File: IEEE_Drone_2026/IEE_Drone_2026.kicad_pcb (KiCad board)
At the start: 4 copper layers, 44.9 x 45.5 mm, 44 parts, among them IC1 TPSM84209RKHT, J1 ESC, J13 USB_C_Receptacle_USB2.0_16P, J2 M4 Mounting, J3 M4 Mounting, J4 M4 Mounting, J5 M4 Mounting, U2 STM32F405RGTx, U3 BMP390, U5 LIS2MDL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

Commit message: slight routing updates
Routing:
- net GND: track 78.0 -> 76.6 mm, vias 24 -> 23
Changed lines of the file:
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@@
-	)
-	(segment
-		(start 85.2086 110.8384)
-		(end 83.853 110.8384)
-		(width 0.7)
-		(layer "F.Cu")
-		(net 1)
 	)
 	(segment
@@
 		(end 95.949062 114.178337)
 		(width 0.3)
-		(layer "F.Cu")
-		(net 1)
-	)
-	(segment
-		(start 83.853 110.8384)
-		(end 83.8494 110.8348)
-		(width 0.7)
 		(layer "F.Cu")
 		(net 1)
@@
 		(size 0.6)
 		(drill 0.3)
-		(layers "F.Cu" "B.Cu")
-		(net 1)
-	)
-	(via
-		(at 83.8494 110.8348)
-		(size 0.6)
-		(drill 0.3)

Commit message: slight routing updates
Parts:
- moved C8 1.09 mm to (90.3, 111.4), turned to 0 degrees
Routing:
- net Net-(U2-PC14): track 4.42 -> 2.35 mm
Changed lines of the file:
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@@
 	(footprint "Capacitor_SMD:C_0603_1608Metric_Pad1.08x0.95mm_HandSolder"
 		(layer "F.Cu")
-		(at 89.3042 111.8192 -90)
+		(at 90.297 111.379)
 		(descr "Capacitor SMD 0603 (1608 Metric), square (rectangular) end terminal, IPC-7351 nominal with elongated pad for handsoldering. (Body size source: IPC-SM-782 page 76, https://www.pcb-3d.com/wordpress/wp-content/uploads/ipc-sm-782a_amendment_1_and_2.pdf), generated with kicad-footprint-generator")
 		(tags "capacitor handsolder")
 		(property "Reference" "C8"
-			(at 2.3538 0.0232 180)
+			(at -0.127 1.524 180)
 			(layer "F.SilkS")
 			(effects
@@
 		)
 		(property "Value" "12pF"
-			(at 0 1.43 90)
+			(at 0 1.43 0)
 			(layer "F.Fab")
 			(hide yes)
@@
 		)
 		(property "Datasheet" "~"
-			(at 0 0 90)
+			(at 0 0 0)
 			(layer "F.Fab")
 			(hide yes)
@@
 		)
 		(property "Description" "Unpolarized capacitor"
-			(at 0 0 90)
+			(at 0 0 0)
 			(layer "F.Fab")
 			(hide yes)
@@
 		(attr smd)
 		(fp_line
-			(start -0.146267 0.51)
-			(end 0.146267 0.51)
+			(start -0.146267 -0.51)
+			(end 0.146267 -0.51)
 			(stroke
 				(width 0.12)
@@
 		)
 		(fp_line
-			(start -0.146267 -0.51)
-			(end 0.146267 -0.51)
+			(start -0.146267 0.51)
+			(end 0.146267 0.51)
 			(stroke
 				(width 0.12)
@@
 		)
 		(fp_line
-			(start -1.65 0.73)
-			(end -1.65 -0.73)
+			(start -1.65 -0.73)
+			(end 1.65 -0.73)
 			(stroke
 				(width 0.05)
@@
 		)
 		(fp_line
-			(start 1.65 0.73)
-			(end -1.65 0.73)
+			(start -1.65 0.73)
+			(end -1.65 -0.73)
 			(stroke
 				(width 0.05)
@@
 		)
 		(fp_line
-			(start -1.65 -0.73)
-			(end 1.65 -0.73)
+			(start 1.65 -0.73)
+			(end 1.65 0.73)
 			(stroke
 				(width 0.05)
@@
 		)
 		(fp_line
-			(start 1.65 -0.73)
-			(end 1.65 0.73)
+			(start 1.65 0.73)
+			(end -1.65 0.73)
 			(stroke
 				(width 0.05)
@@
 		)
 		(fp_line
-			(start -0.8 0.4)
-			(end -0.8 -0.4)
+			(start -0.8 -0.4)
+			(end 0.8 -0.4)
 			(stroke
 				(width 0.1)
@@
 		)
 		(fp_line
-			(start 0.8 0.4)
-			(end -0.8 0.4)
+			(start -0.8 0.4)
+			(end -0.8 -0.4)
 			(stroke
 				(width 0.1)
@@
 		)
 		(fp_line
-			(start -0.8 -0.4)
-			(end 0.8 -0.4)
+			(start 0.8 -0.4)
+			(end 0.8 0.4)
 			(stroke
 				(width 0.1)
@@
 		)
 		(fp_line
-			(start 0.8 -0.4)
-			(end 0.8 0.4)
+			(start 0.8 0.4)
+			(end -0.8 0.4)
 			(stroke
 				(width 0.1)
@@
 		)
 		(fp_text user "${REFERENCE}"
-			(at 0 0 90)
+			(at 0 0 0)
 			(layer "F.Fab")
 			(effects
@@
 		)
 		(pad "1" smd roundrect
-			(at -0.8625 0 270)
+			(at -0.8625 0)
 			(size 1.075 0.95)
 			(layers "F.Cu" "F.Mask" "F.Paste")
@@
 		)
 		(pad "2" smd roundrect
-			(at 0.8625 0 270)
+			(at 0.8625 0)
 			(size 1.075 0.95)
 			(layers "F.Cu" "F.Mask" "F.Paste")
@@
 	)
 	(segment
-		(start 87.6086 110.8384)
-		(end 89.1859 110.8384)
-		(width 0.3)
+		(start 88.1492 111.379)
+		(end 87.6086 110.8384)
+		(width 0.2)
 		(layer "F.Cu")
 		(net 8)
 	)
 	(segment
+		(start 89.4345 111.379)
+		(end 88.1492 111.379)
+		(width 0.2)
+		(layer "F.Cu")
+		(net 8)
+	)
+	(segment
+		(start 91.1595 110.8264)
+		(end 91.1595 111.379)
+		(width 0.3)
+		(layer "F.Cu")
+		(net 9)
+	)
+	(segment
 		(start 91.615 110.3709)
-		(end 89.3042 112.6817)
+		(end 91.1595 110.8264)
 		(width 0.3)
 		(layer "F.Cu")

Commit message: complete redesign
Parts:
- removed BOOT0, NRST: TestPoint, TestPoint:TestPoint_Loop_D2.50mm_Drill1.0mm
- GPS1: footprint Connector_PinHeader_2.54mm:PinHeader_1x04_P2.54mm_Vertical -> Connector_JST:JST_SH_BM04B-SRSS-TB_1x04-1MP_P1.00mm_Vertical
- Pixy1: footprint Connector_PinSocket_2.54mm:PinSocket_1x05_P2.54mm_Vertical -> Connector_JST:JST_SH_BM05B-SRSS-TB_1x05-1MP_P1.00mm_Vertical
- RF1: footprint Connector_PinHeader_2.54mm:PinHeader_1x08_P2.54mm_Vertical -> Connector_JST:JST_SH_BM09B-SRSS-TB_1x09-1MP_P1.00mm_Vertical
- moved GPS1 96.3 mm to (156.7, 138.6), turned to -90 degrees
- moved C19 90.0 mm to (150.4, 153.5), turned to 180 degrees
- moved C22 89.7 mm to (150.4, 155.0), turned to 180 degrees
- moved C16 82.5 mm to (153.9, 144.6)
- moved Y2 81.1 mm to (157.4, 152.4), turned to 90 degrees
- moved C8 80.1 mm to (156.6, 156.4), turned to 180 degrees
- moved C18 78.5 mm to (150.0, 138.2), turned to 0 degrees
- moved C7 77.5 mm to (157.6, 148.3), turned to 180 degrees
- moved R8 76.5 mm to (131.5, 154.0), turned to 180 degrees
- moved C15 75.3 mm to (140.2, 152.0)
- moved R6 73.6 mm to (130.5, 149.5), turned to -90 degrees
- moved Pixy1 73.2 mm to (135.5, 130.3), turned to 0 degrees
- moved C20 71.3 mm to (137.8, 149.2)
- moved J13 71.3 mm to (124.2, 152.7), turned to -90 degrees
- moved J3 69.5 mm to (122.2, 129.9)
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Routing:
- net +3.3V: track 103.1 -> 64.6 mm, vias 16 -> 15
- net /MISO: track 67.9 -> 29.9 mm, vias 2 -> 4
- net /MOSI: track 71.7 -> 40.5 mm
- net /PB12: track 50.3 -> 20.3 mm, vias 3 -> 4
- net +VDC: track 77.7 -> 50.2 mm
- net /SCK: track 41.9 -> 16.1 mm, vias 4 -> 0
- net /TX: track 30.5 -> 5.37 mm, vias 1 -> 0
- net /RX: track 30.2 -> 6.00 mm, vias 1 -> 0
- net GND: track 76.6 -> 98.1 mm, vias 23 -> 26
- net /PB13: track 40.8 -> 19.4 mm, vias 4 -> 2
- net /PB3: track 40.1 -> 18.7 mm, vias 0 -> 3
- net /SCK (SPI3): track 37.8 -> 56.8 mm, vias 2 -> 4
- net Net-(U2-NRST): track 17.6 -> 0.00 mm, vias 1 -> 0
- net /PB8: track 18.7 -> 5.91 mm, vias 2 -> 0
- net /PB0: track 35.3 -> 25.6 mm
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- added copper zone on In1.Cu, net +3.3V
- removed copper zone on B.Cu, net GND
- removed copper zone on F.Cu, net GND
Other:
- board size 44.9 x 45.5 mm -> 39.5 x 40 mm

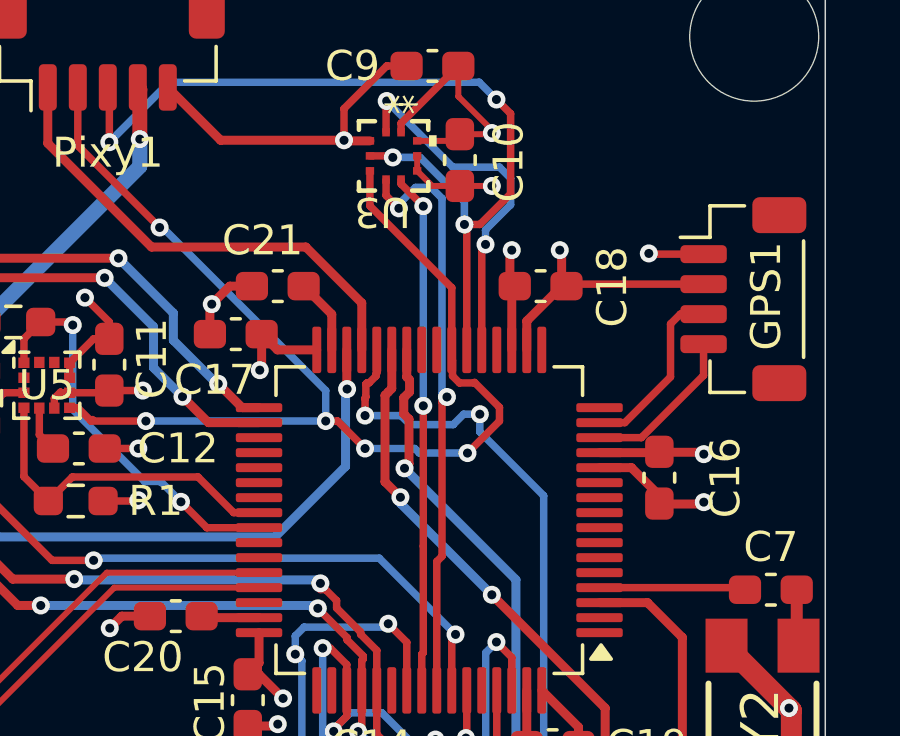
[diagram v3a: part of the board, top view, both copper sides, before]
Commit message: updated silkscreen
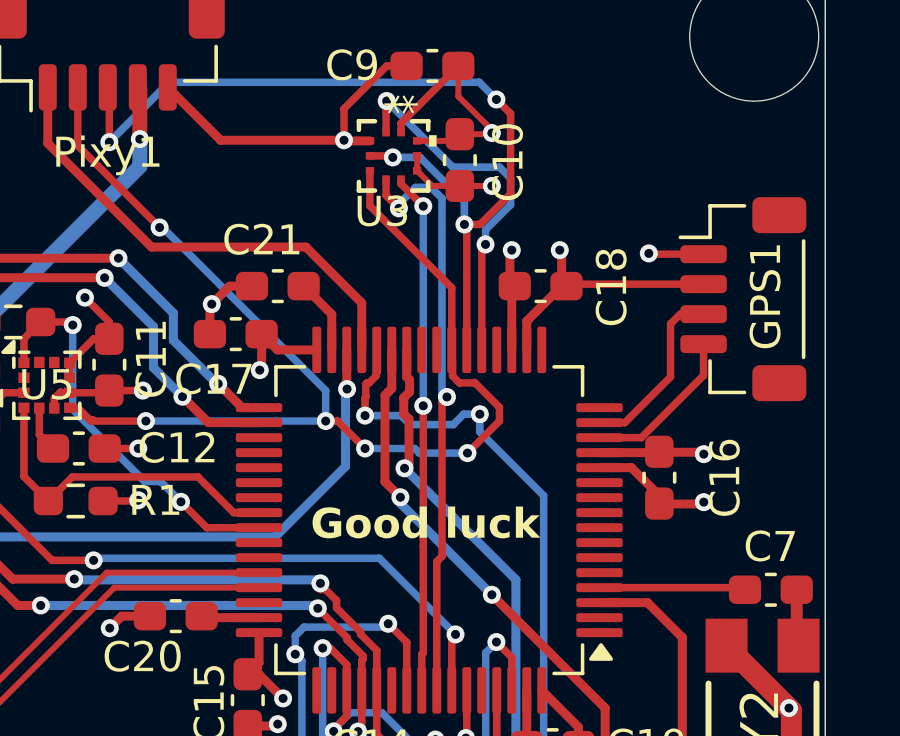
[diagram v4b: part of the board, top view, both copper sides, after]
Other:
- board text added: "Good luck"
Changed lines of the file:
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@@
 		(tags "BMP390 ")
 		(property "Reference" "U3"
-			(at 1.8688 0.377 180)
+			(at 1.8688 0.377 0)
 			(unlocked yes)
 			(layer "F.SilkS")
@@
 		(layer "Edge.Cuts")
 	)
+	(gr_text "Good luck"
+		(at 142.2908 146.7104 0)
+		(layer "F.SilkS")
+		(effects
+			(font
+				(size 1 1)
+				(thickness 0.25)
+				(bold yes)
+			)
+			(justify left bottom)
+		)
+	)
 	(segment

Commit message: added my name
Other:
- board text added: "Hermes Made by Caleb Murray"
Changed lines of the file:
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@@
+		)
+	)
+	(gr_text "Hermes\nMade by Caleb Murray\n"
+		(at 152.2984 132.1308 0)
+		(layer "B.SilkS")
+		(effects
+			(font
+				(size 1.5 1.5)
+				(thickness 0.3)
+				(bold yes)
+			)
+			(justify left bottom mirror)
 		)
 	)

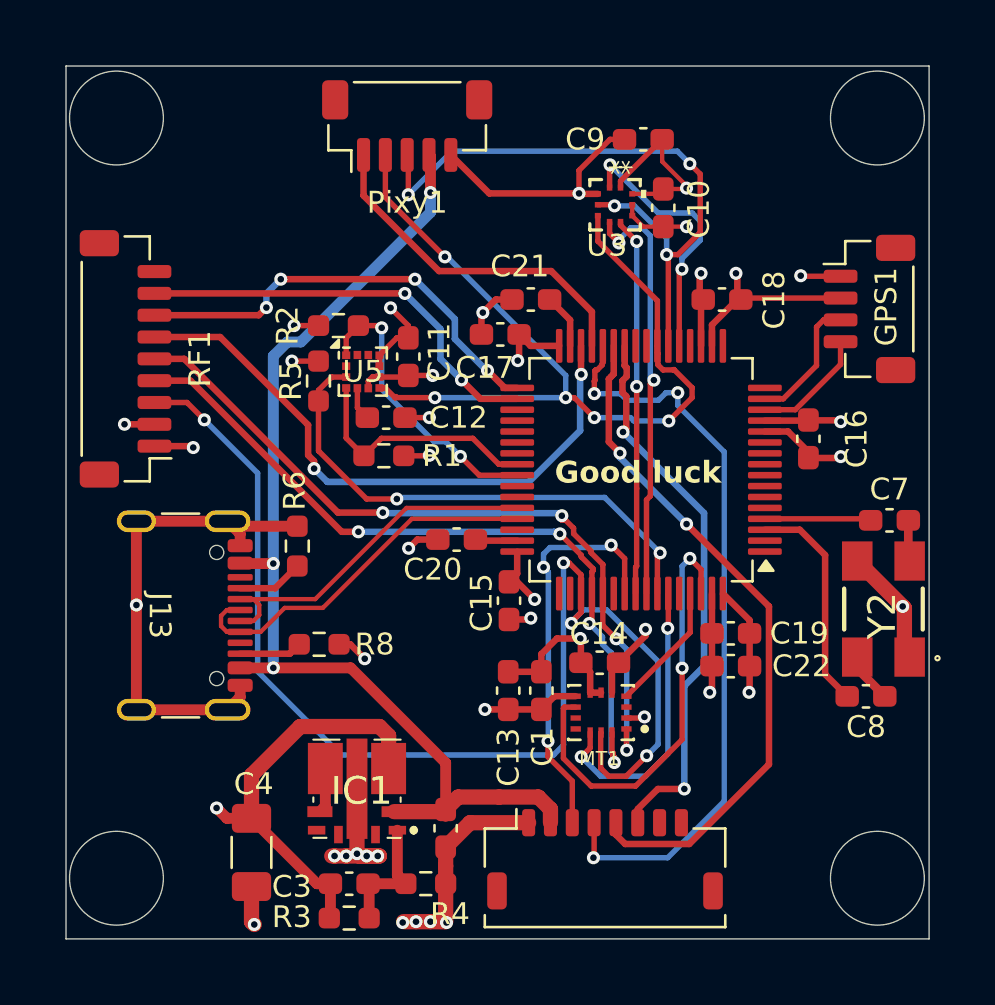
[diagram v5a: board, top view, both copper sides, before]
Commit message: added chamfered edges
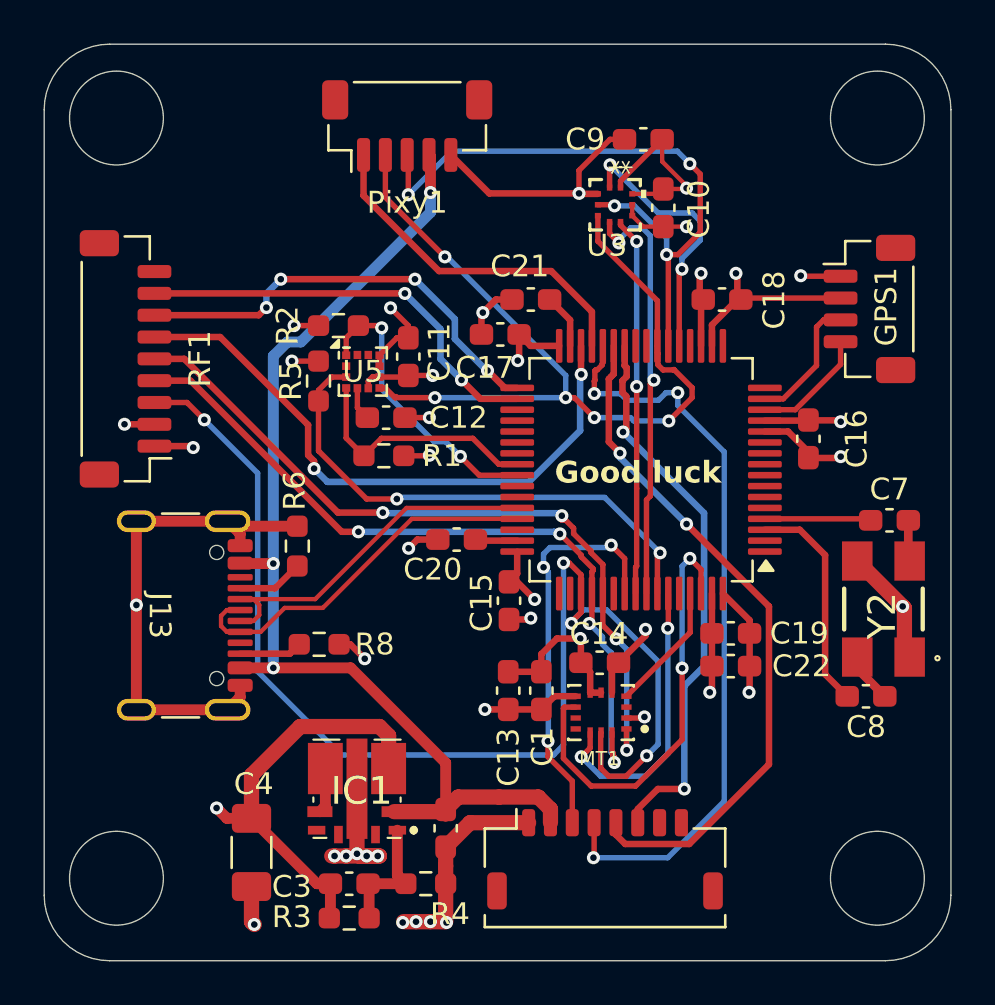
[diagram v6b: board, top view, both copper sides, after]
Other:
- board size 39.5 x 40 mm -> 41.5 x 42 mm
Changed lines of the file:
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@@
 		)
 	)
-	(gr_rect
-		(start 119.9 127.5)
-		(end 159.45 167.5)
+	(gr_arc
+		(start 121.9 168.5)
+		(mid 119.77868 167.62132)
+		(end 118.9 165.5)
 		(stroke
 			(width 0.05)
 			(type default)
 		)
-		(fill no)
 		(layer "Edge.Cuts")
 	)
+	(gr_line
+		(start 121.9 126.5)
+		(end 157.45 126.5)
+		(stroke
+			(width 0.05)
+			(type default)
+		)
+		(layer "Edge.Cuts")
+	)
+	(gr_arc
+		(start 160.45 165.5)
+		(mid 159.57132 167.62132)
+		(end 157.45 168.5)
+		(stroke
+			(width 0.05)
+			(type default)
+		)
+		(layer "Edge.Cuts")
+	)
+	(gr_line
+		(start 118.9 165.5)
+		(end 118.9 129.5)
+		(stroke
+			(width 0.05)
+			(type default)
+		)
+		(layer "Edge.Cuts")
+	)
+	(gr_line
+		(start 160.45 129.5)
+		(end 160.45 165.5)
+		(stroke
+			(width 0.05)
+			(type default)
+		)
+		(layer "Edge.Cuts")
+	)
+	(gr_line
+		(start 157.45 168.5)
+		(end 121.9 168.5)
+		(stroke
+			(width 0.05)
+			(type default)
+		)
+		(layer "Edge.Cuts")
+	)
+	(gr_arc
+		(start 118.9 129.5)
+		(mid 119.77868 127.37868)
+		(end 121.9 126.5)
+		(stroke
+			(width 0.05)
+			(type default)
+		)
+		(layer "Edge.Cuts")
+	)
+	(gr_arc
+		(start 157.45 126.5)
+		(mid 159.57132 127.37868)
+		(end 160.45 129.5)
+		(stroke
+			(width 0.05)
+			(type default)
+		)
+		(layer "Edge.Cuts")
+	)

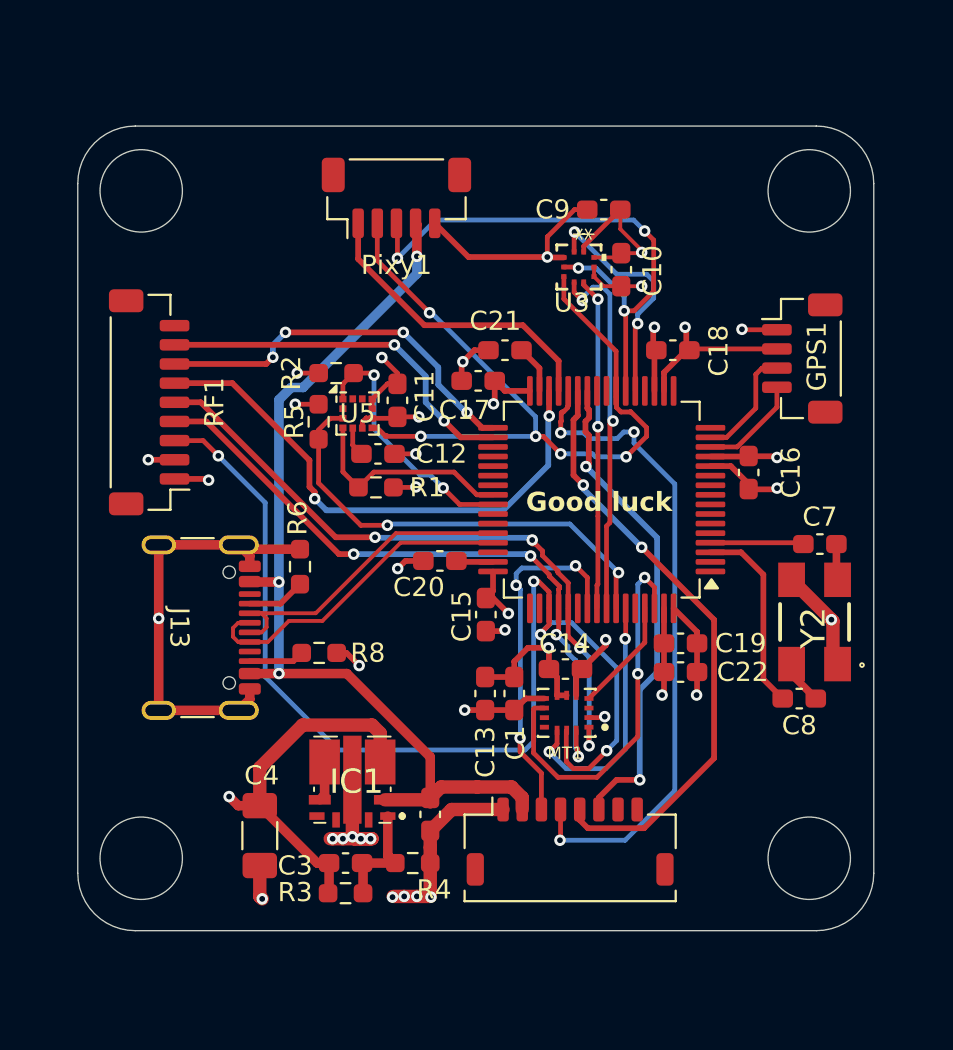
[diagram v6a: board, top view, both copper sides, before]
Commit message: added bottom layer gnd plane
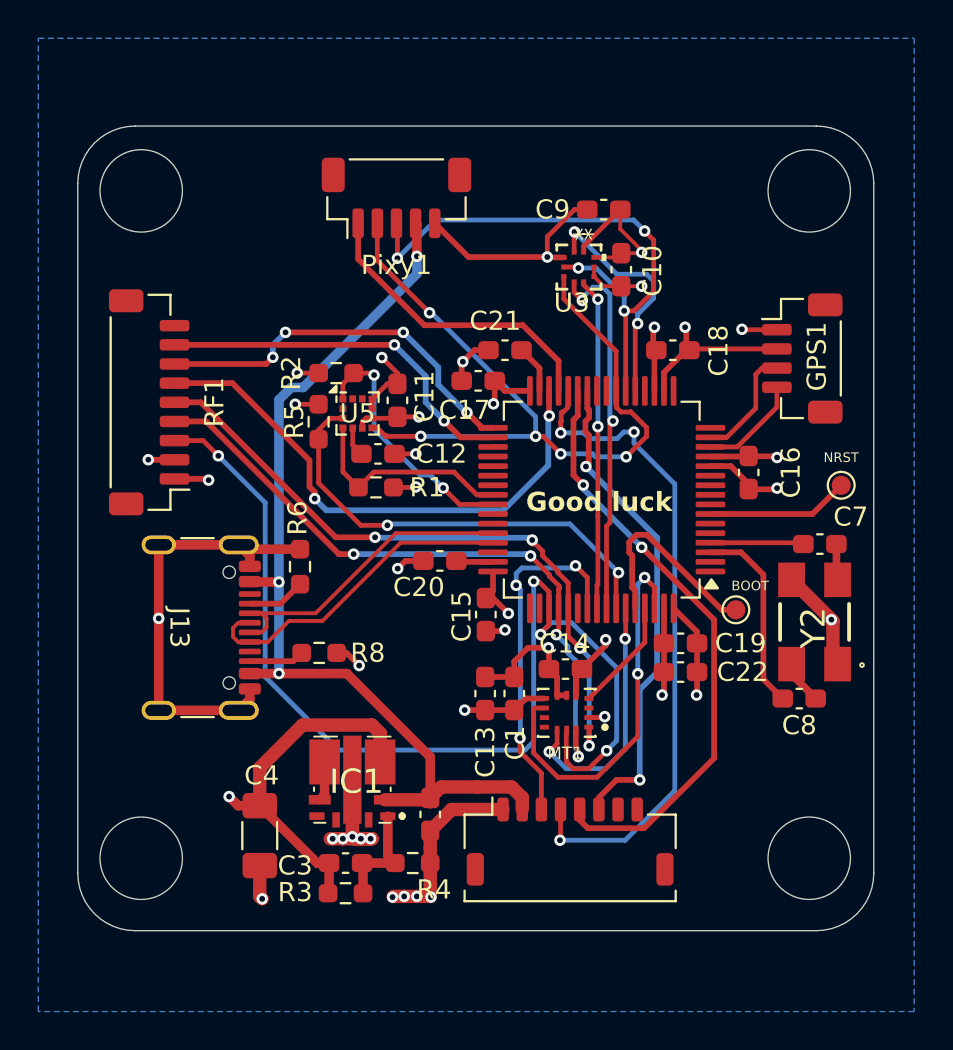
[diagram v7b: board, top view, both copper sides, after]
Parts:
- added BOOT: TestPoint, TestPoint:TestPoint_Pad_D1.0mm, F.Cu at (153.2, 151.8)
- added NRST: TestPoint, TestPoint:TestPoint_Pad_D1.0mm, F.Cu at (158.8, 145.2)
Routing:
- net Net-(U2-BOOT0): track 0.00 -> 10.9 mm
- net Net-(U2-NRST): track 0.00 -> 7.45 mm
- added copper zone on B.Cu, net GND
